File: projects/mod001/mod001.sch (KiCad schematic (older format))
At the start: 14 parts, among them U1 LD1117S33TR, U2 SFC_MaskRom_32pin_SOCKET, U3 74LVC245, U4 74LVC245, U5 74LVC245, U6 SST39VF1681_1682

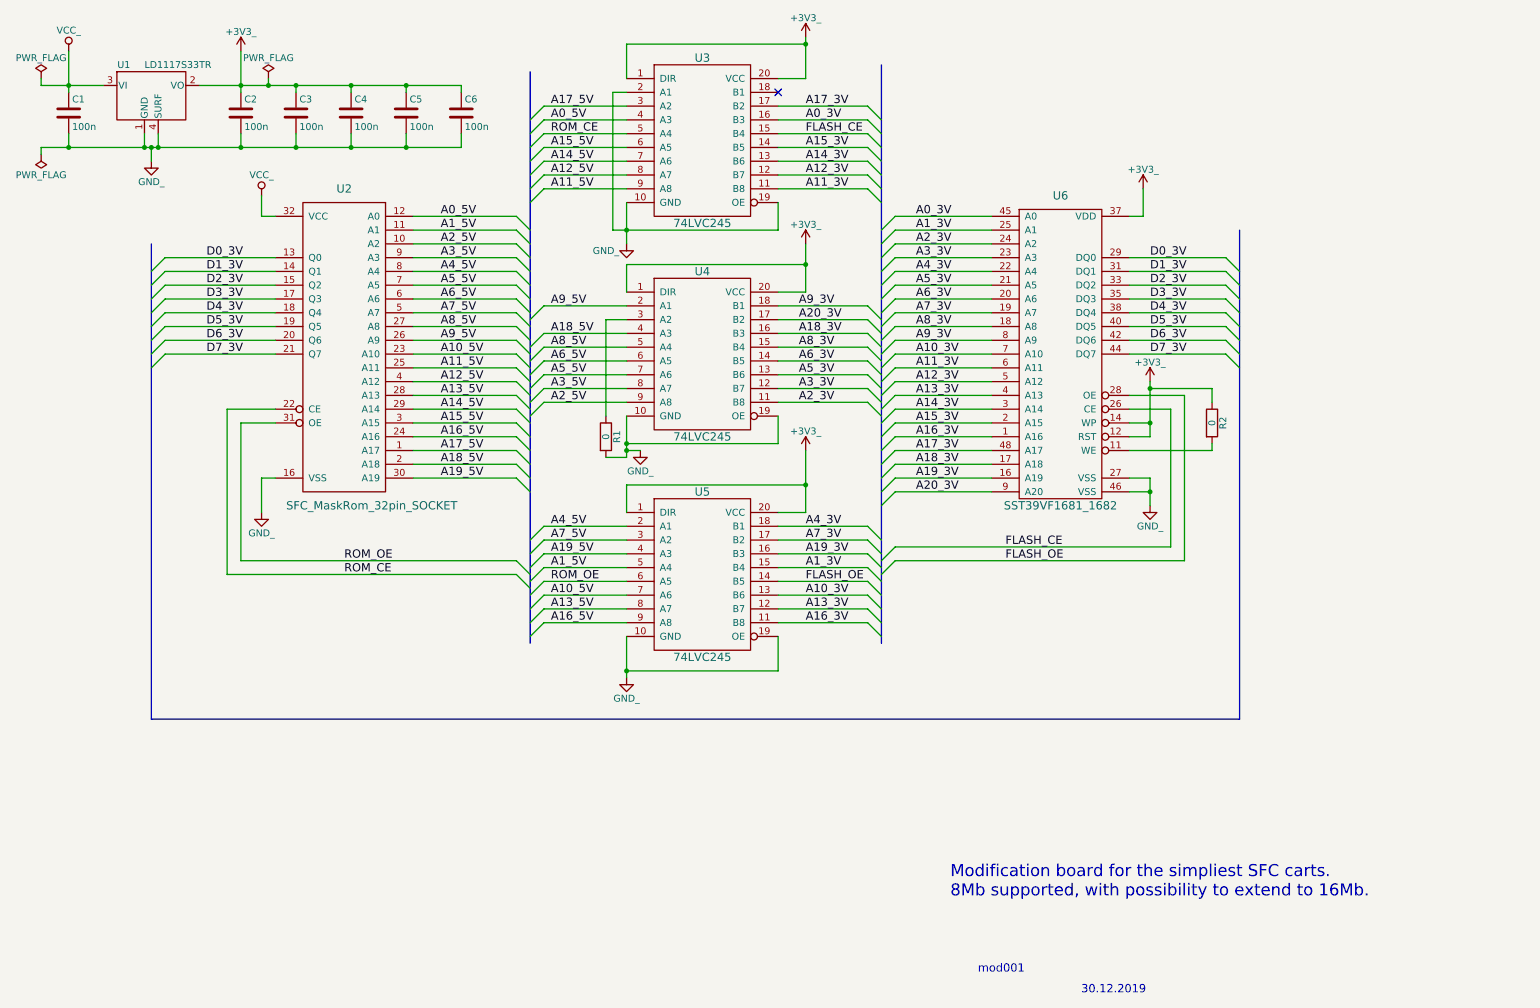
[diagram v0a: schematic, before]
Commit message: Fixed mod001 (making pin 4 of U1 unconnected).
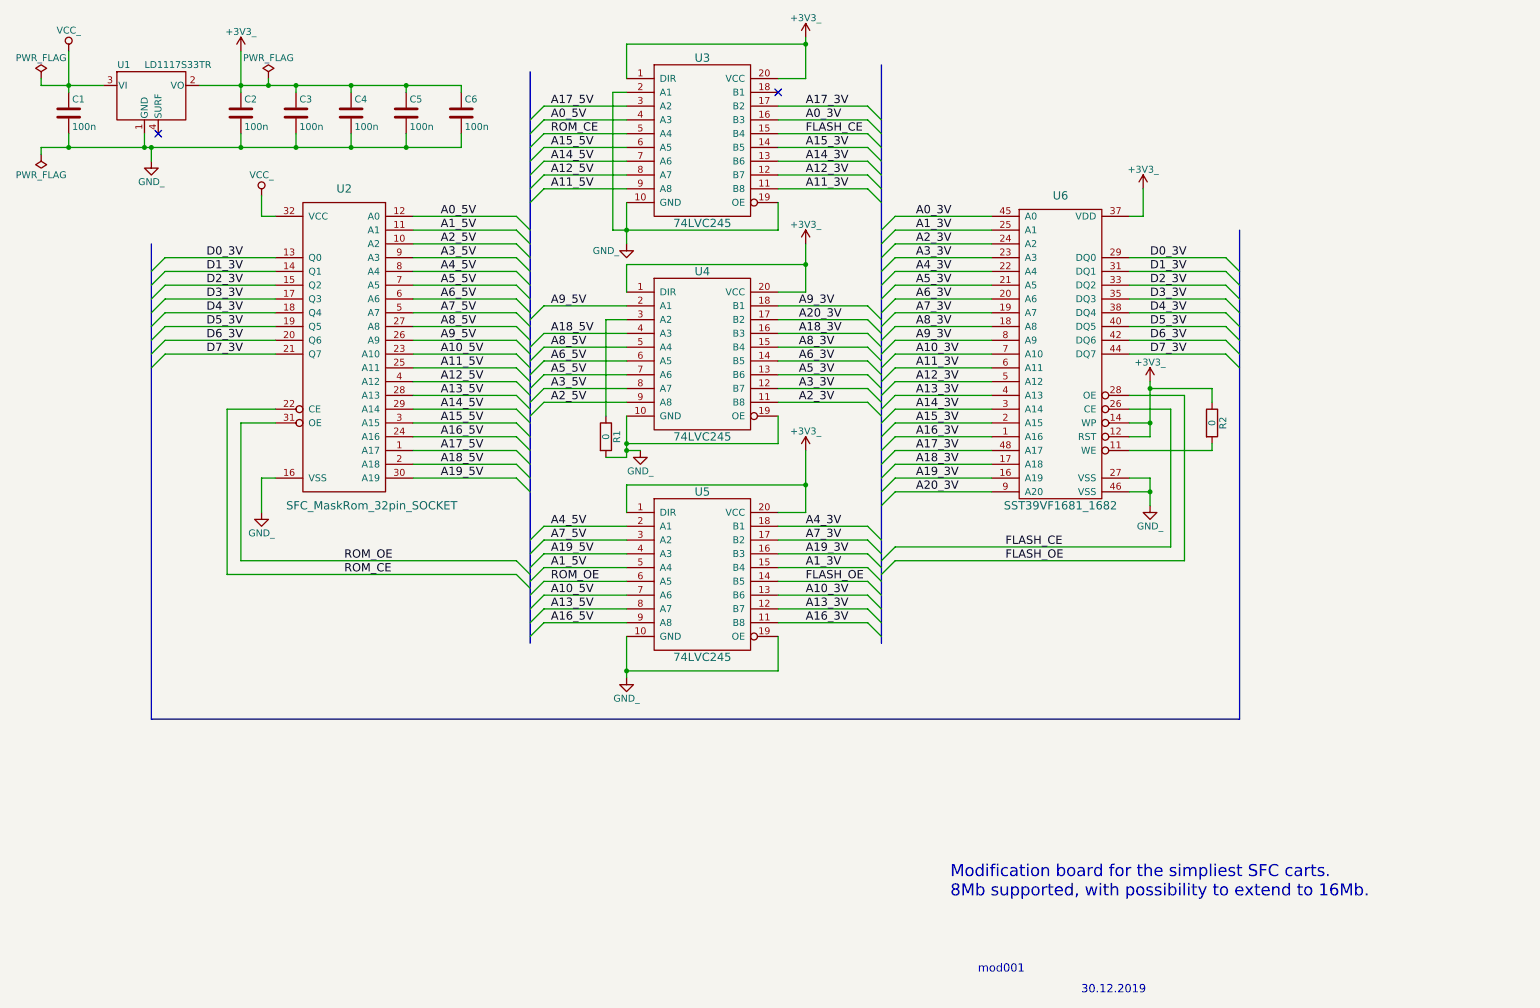
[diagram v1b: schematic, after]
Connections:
- net GND_: no longer U1.4 (SURF)
- no-connect marks 1 -> 2
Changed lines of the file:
@@
 	6900 4000 7600 4000
 Wire Wire Line
-	8600 3500 8750 3500
+	8750 3500 8600 3500
 Wire Wire Line
 	8750 3600 8600 3600
@@
 	2150 800  2150 1100
 Wire Wire Line
-	1450 1400 1450 1500
+	1450 1500 1450 1400
 Wire Wire Line
 	700  1500 3750 1500
-Wire Wire Line
-	1550 1500 1550 1400
 $Comp
 L GND_ #PWR011
@@
 $EndComp
 Wire Wire Line
-	1500 1600 1500 1500
+	1500 1500 1500 1600
 Connection ~ 1500 1500
 $Comp
@@
 Wire Wire Line
 	2150 1500 2150 1400
-Connection ~ 1550 1500
 Entry Wire Line
 	4150 2000 4250 2100
@@
 	8700 2000 8700 1800
 Wire Bus Line
-	9400 5650 9400 2100
+	9400 2100 9400 5650
 Wire Bus Line
-	1500 5650 9400 5650
+	9400 5650 1500 5650
 Wire Bus Line
 	1500 5650 1500 2200
@@
 	9200 3250 8750 3250
 Connection ~ 8750 3250
+NoConn ~ 1550 1400
 $EndSCHEMATC
